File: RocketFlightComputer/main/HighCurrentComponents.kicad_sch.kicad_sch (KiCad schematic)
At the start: 29 parts, among them Q2 SI2302, Q3 SI2302

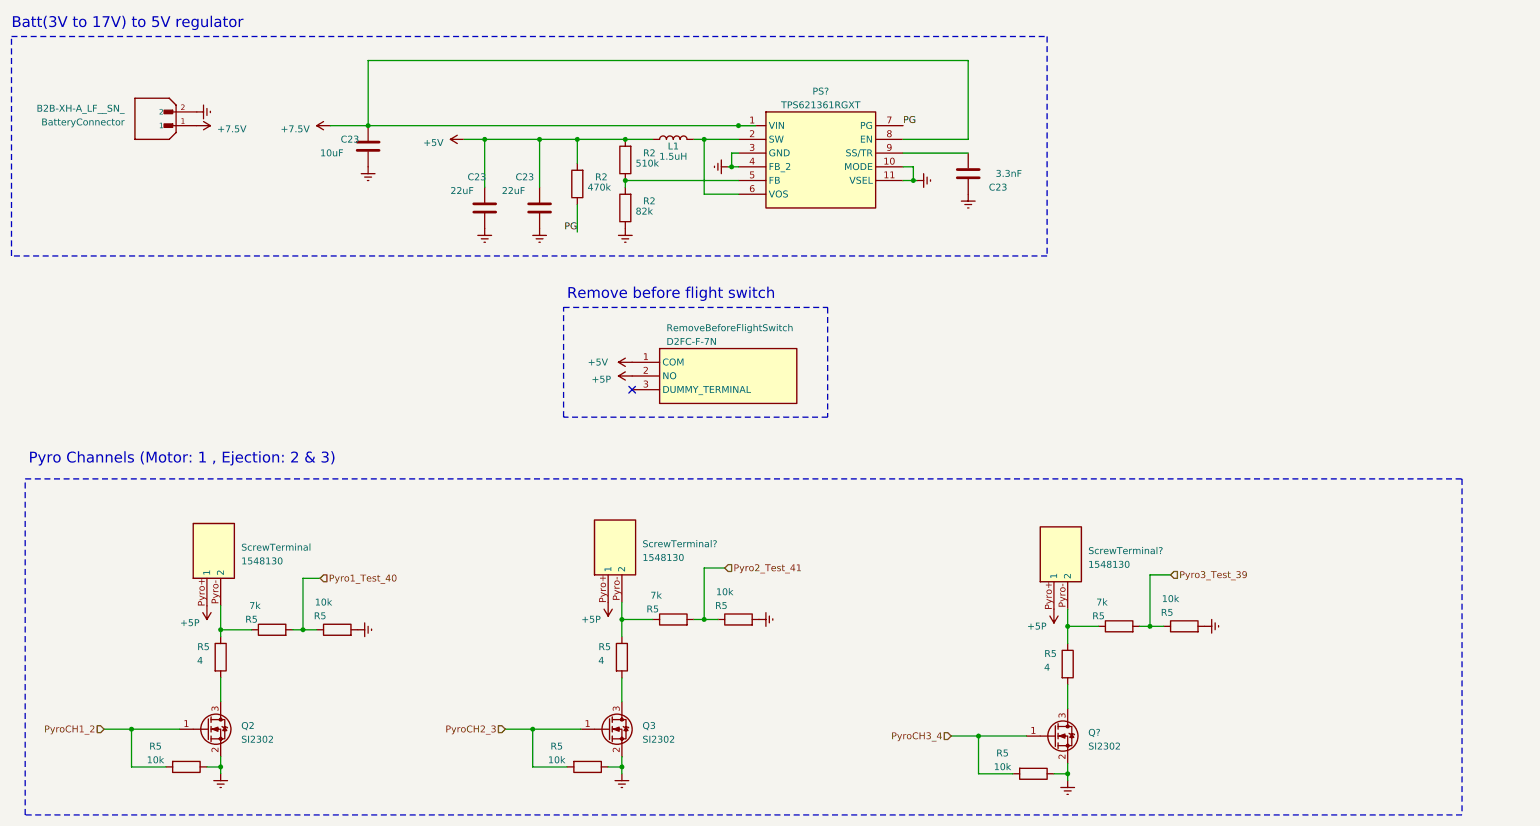
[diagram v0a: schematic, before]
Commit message: Addition of telemetry is pcb schematic
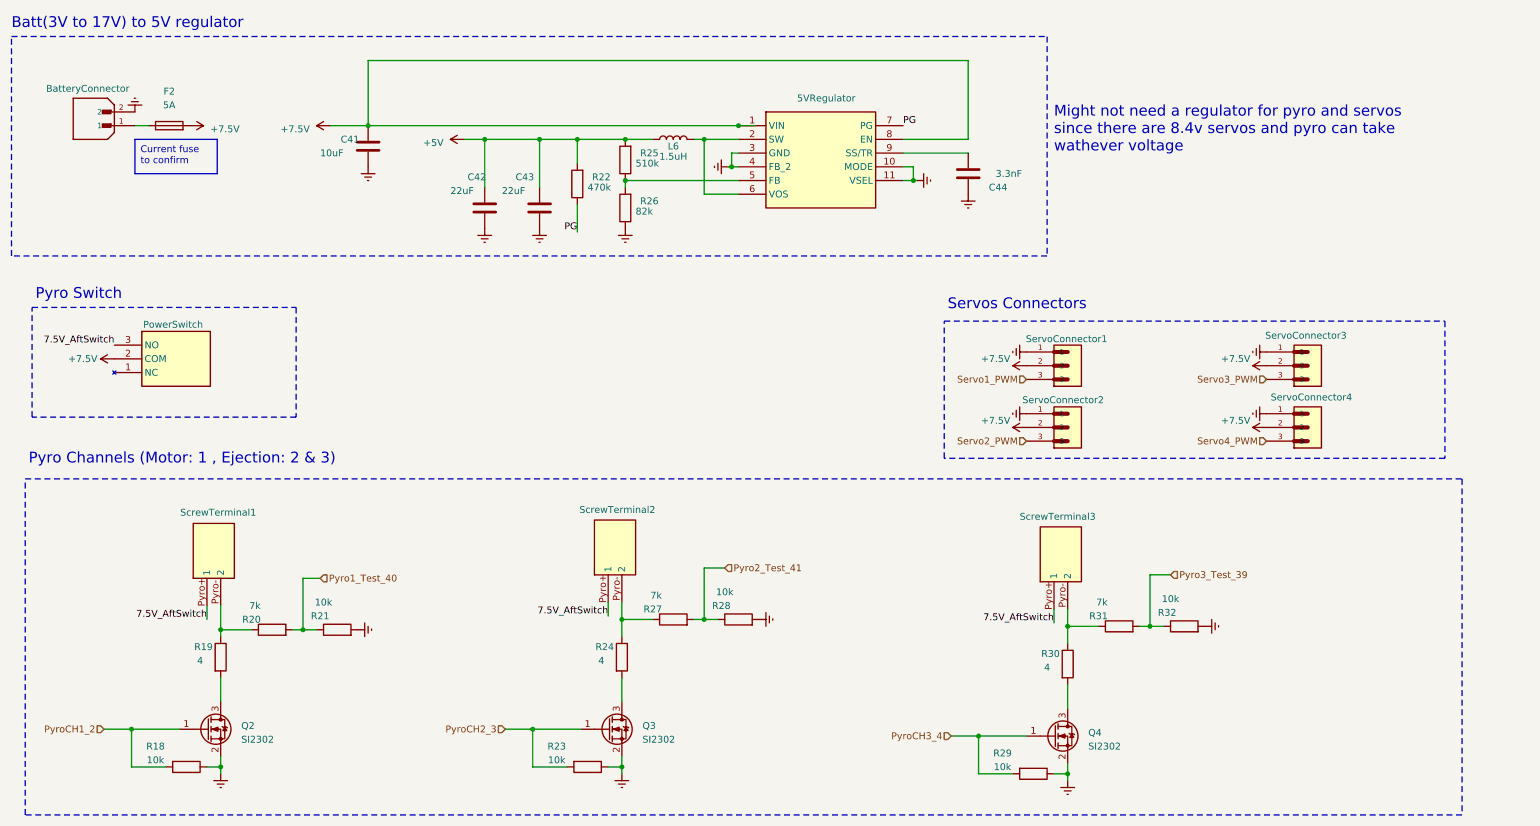
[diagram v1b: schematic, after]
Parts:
- removed RemoveBeforeFlightSwitch: D2FC-F-7N, footprint:D2FCF7N60M, symbol D2FC-F-7N_60M_:D2FC-F-7N_60M_
- added F2: 5A, Resistor_SMD:R_0603_1608Metric_Pad0.98x0.95mm_HandSolder, symbol Device:Fuse
- added PowerSwitch: L102011MS02Q, PowerButton:L102011MS02Q, symbol L102011MS02Q:L102011MS02Q
- added ServoConnector1, ServoConnector2, ServoConnector3, ServoConnector4: B3P-VH_LF__SN_, footprint:JST_B3P-VH_LF__SN_, symbol B3P-VH_LF__SN_:B3P-VH_LF__SN_
- gave numbers to parts that had none: 4
- renumbered C23 to C41, C23 to C42, C23 to C43, C23 to C44, L1 to L6, R5 to R18, R5 to R19, R5 to R20, R5 to R21, R2 to R22, R5 to R23, R5 to R24, R2 to R25, R2 to R26, R5 to R27, R5 to R28, R5 to R29, R5 to R30, R5 to R31, R5 to R32, ScrewTerminal to ScrewTerminal1
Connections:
- net +7.5V: now also F2.2, PowerSwitch.2 (COM), ServoConnector1.2, ServoConnector2.2, ServoConnector3.2, ServoConnector4.2; no longer BatteryConnector.1
- net GNDREF: now also ServoConnector1.1, ServoConnector2.1, ServoConnector3.1, ServoConnector4.1
- net +5P renamed 7.5V_AftSwitch
- net 7.5V_AftSwitch: now also PowerSwitch.3 (NO)
- new net: BatteryConnector.1, F2.1
- new net Servo1_PWM: ServoConnector1.3
- new net Servo2_PWM: ServoConnector2.3
- new net Servo3_PWM: ServoConnector3.3
- new net Servo4_PWM: ServoConnector4.3
- no-connect marks 1 -> 0
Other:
- note added: "Might not need a regulator for pyro and servos since there are 8.4v servos and pyro can take wathever voltage"
- note added: "Pyro Switch"
- note added: "Servos Connectors"
- note removed: "Remove before flight switch"
- moved on the sheet: BatteryConnector

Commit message: The design is getting more mature, still did not choose if doing 4 layers or 2 layers pcb, will try to add 5v for a on board camera and trace routes for reserved pins in case of usage on another vehicle
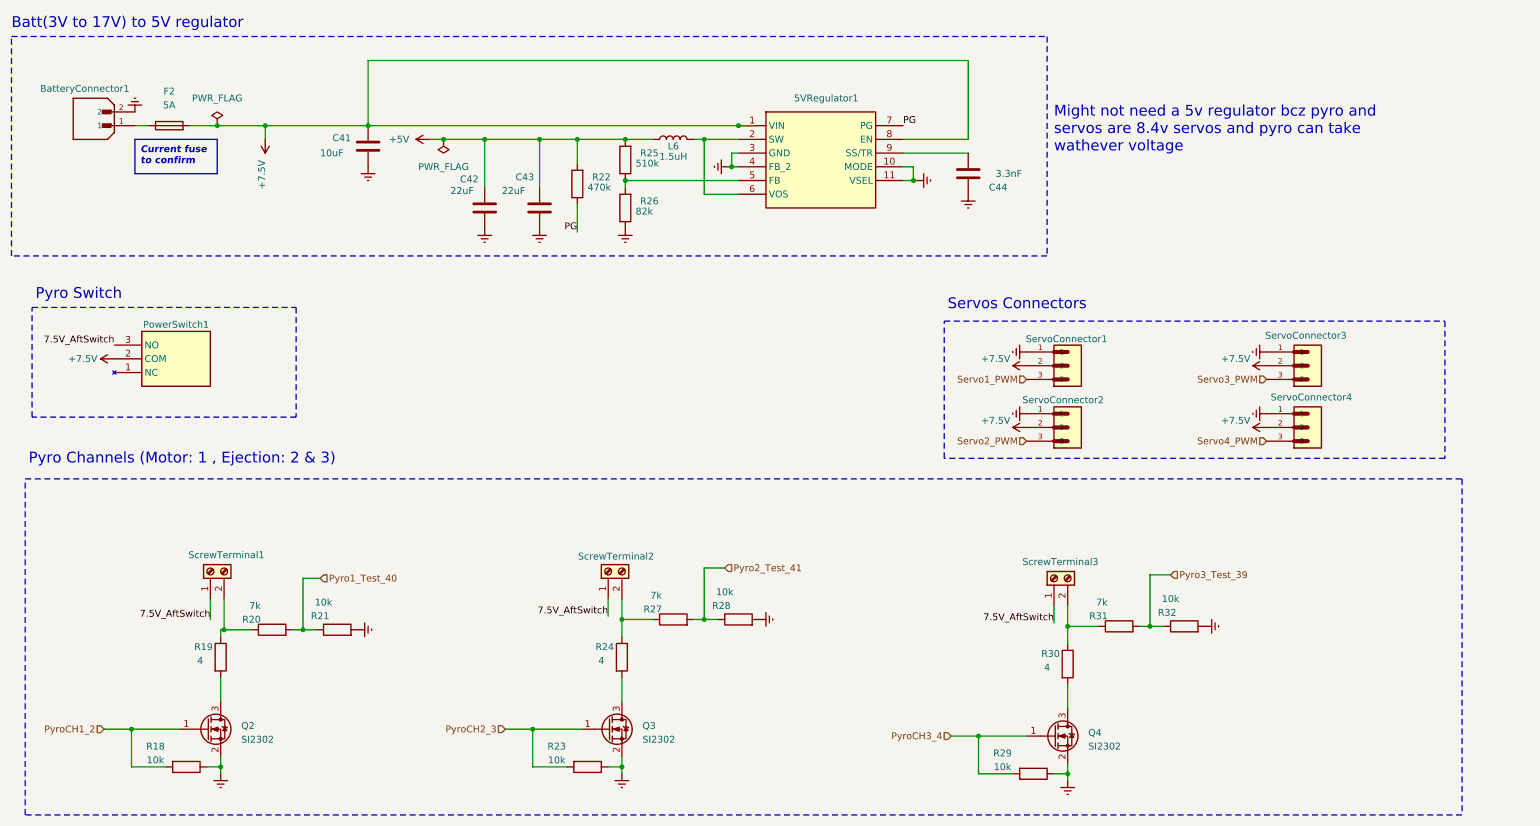
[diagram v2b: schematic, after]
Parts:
- removed ScrewTerminal1, ScrewTerminal2, ScrewTerminal3: 1548130, footprint:1548130, symbol 1548130:1548130
- added ScrewTerminal1, ScrewTerminal2, ScrewTerminal3: Screw_Terminal_01x02, ScrewTerminals:2.54mm, symbol Connector:Screw_Terminal_01x02
- 5VRegulator1: renamed from 5VRegulator; footprint TPS621361RGXT -> footprint:TPS621361RGXT
- L6: footprint (none) -> Resistor_SMD:R_0603_1608Metric_Pad0.98x0.95mm_HandSolder
- renumbered BatteryConnector to BatteryConnector1, PowerSwitch to PowerSwitch1
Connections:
- net 7.5V_AftSwitch: now also ScrewTerminal1.1 (Pyro+), ScrewTerminal2.1 (Pyro+), ScrewTerminal3.1 (Pyro+)
- net at R30.1, R31.1: now also ScrewTerminal3.2 (Pyro-)
- net at R19.1, R20.1: now also ScrewTerminal1.2 (Pyro-)
- net at R24.1, R27.1: now also ScrewTerminal2.2 (Pyro-)
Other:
- note added: "Might not need a 5v regulator bcz pyro and servos are 8.4v servos and pyro can take wathever voltage"
- note removed: "Might not need a regulator for pyro and servos since there are 8.4v servos and pyro can take wathever voltage"

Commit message: Camera and reserve
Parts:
- removed BatteryConnector1: B2B-XH-A_LF__SN_, footprint:JST_B2B-XH-A_LF__SN_, symbol B2B-XH-A_LF__SN_:B2B-XH-A_LF__SN_
- removed PowerSwitch1: L102011MS02Q, PowerButton:L102011MS02Q, symbol L102011MS02Q:L102011MS02Q
- added BatteryConnector1: XT30UPB-M, XT30:AMASS_XT30UPB-M, symbol xt30:XT30UPB-M
- added ScrewTerminal4: Screw_Terminal_01x02, ScrewTerminals:2.54mm, symbol Connector:Screw_Terminal_01x02
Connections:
- net +7.5V: now also ScrewTerminal4.2 (Pyro-); no longer F2.2
- net 7.5V_AftSwitch: now also ScrewTerminal4.1 (Pyro+)
- net GNDREF: now also BatteryConnector1.N
- net at F2.1: now also BatteryConnector1.P
- new net +BATT: F2.2

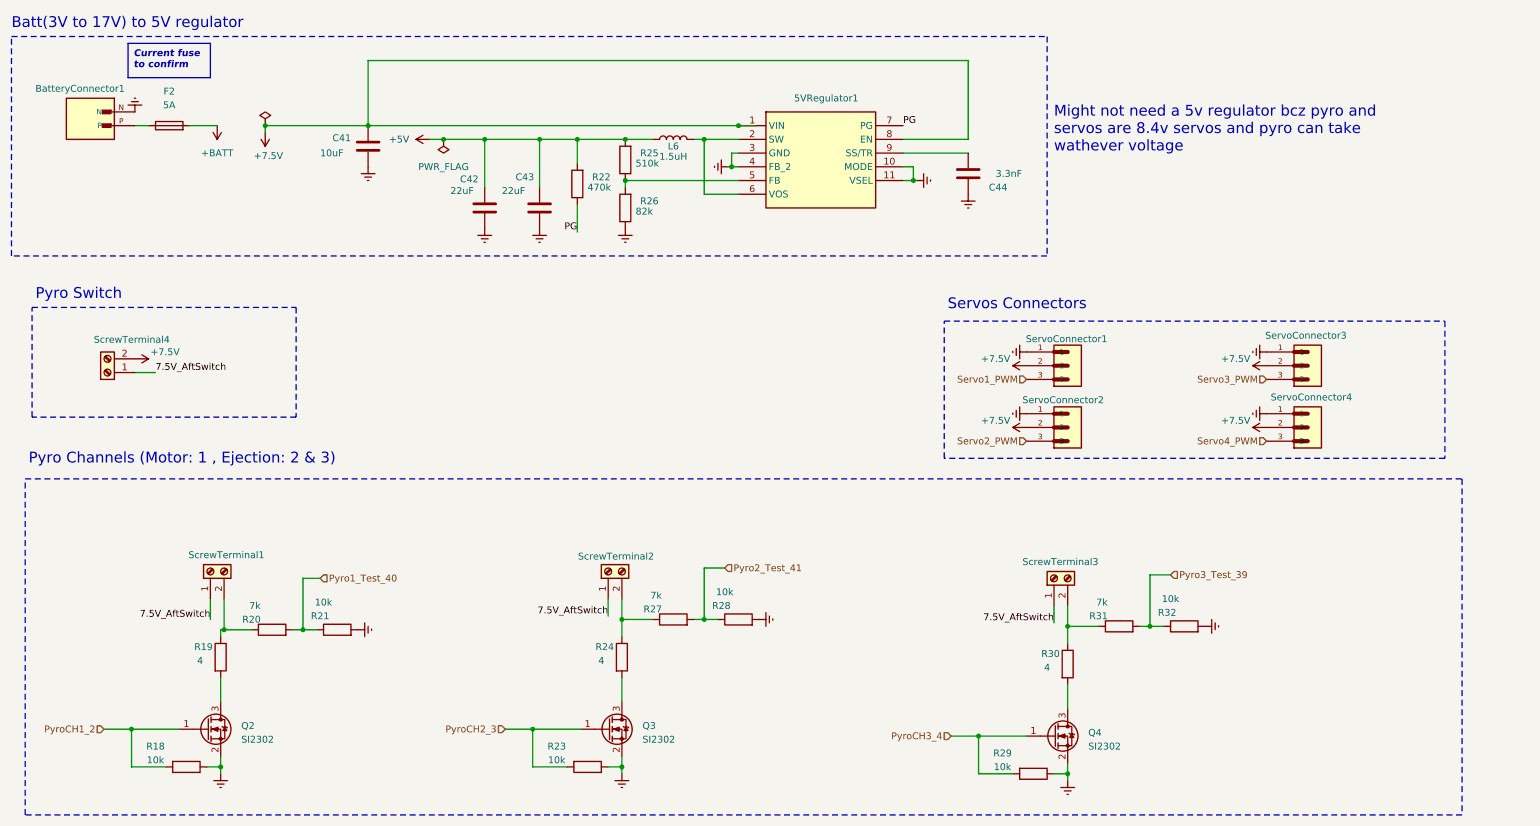
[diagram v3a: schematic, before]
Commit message: CID documentation and started the PCB editor process
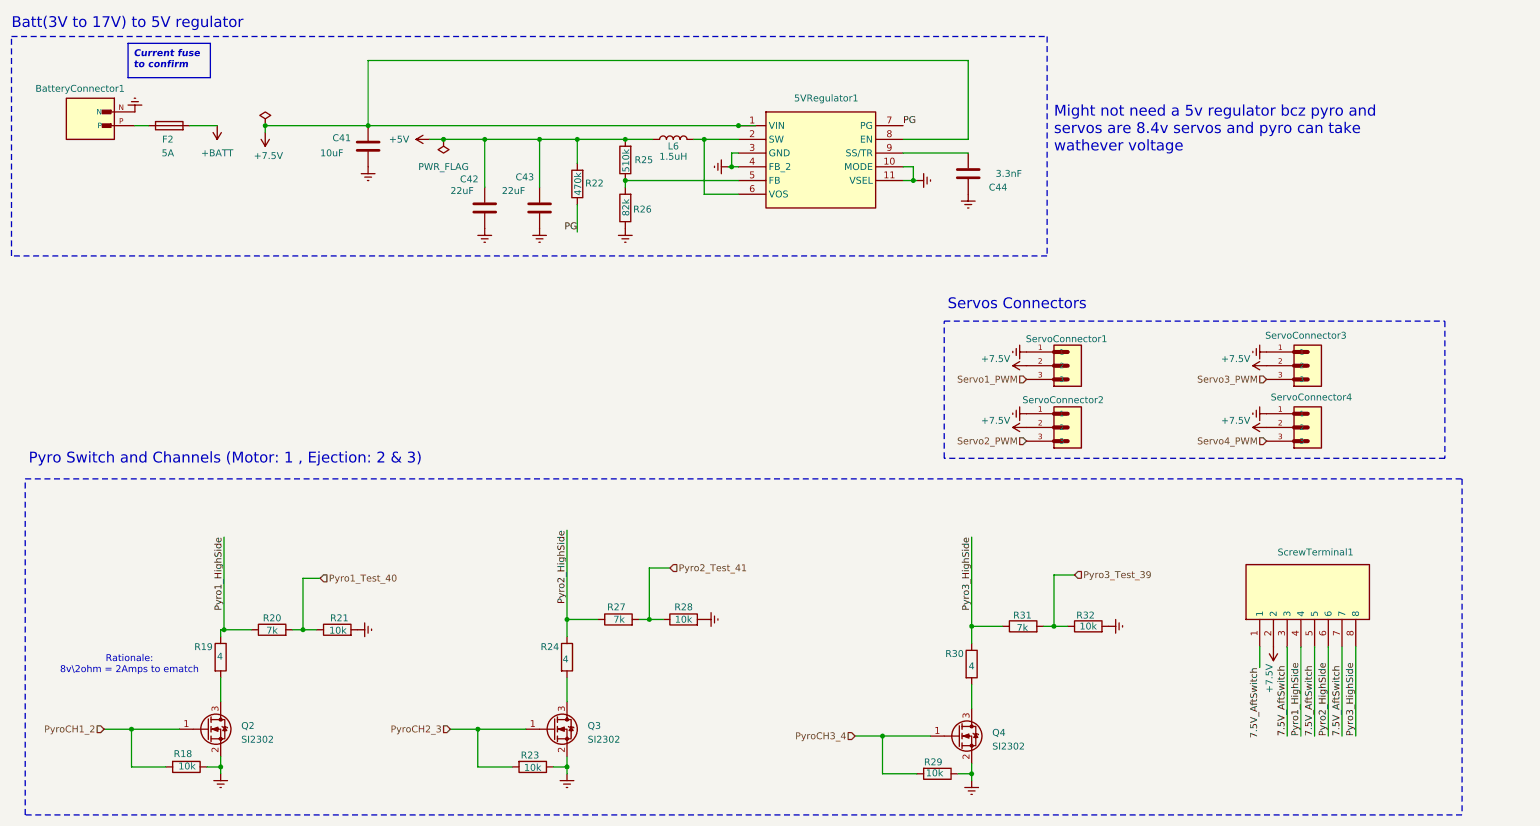
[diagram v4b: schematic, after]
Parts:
- removed ScrewTerminal1, ScrewTerminal2, ScrewTerminal3, ScrewTerminal4: Screw_Terminal_01x02, ScrewTerminals:2.54mm, symbol Connector:Screw_Terminal_01x02
- added ScrewTerminal1: 1725711, footprint:1725711, symbol 1725711:1725711
- ServoConnector1, ServoConnector2, ServoConnector4: value B3P-VH_LF__SN_ -> ~; footprint footprint:JST_B3P-VH_LF__SN_ -> Connector_JST:JST_GH_BM03B-GHS-TBT_1x03-1MP_P1.25mm_Vertical; Availability In Stock -> (none); Check_prices https://www.snapeda.com/parts/B3P-VH(LF)(SN)/JST+Sales+Amer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 -> (none); MANUFACTURER JST -> (none); MF JST Sales -> (none); MP B3P-VH(LF)(SN) -> (none); Package None -> (none); Price None -> (none); SnapEDA_Link https://www.snapeda.com/parts/B3P-VH(LF)(SN)/JST+Sales+Amer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 -> (none)
- ServoConnector3: value B3P-VH_LF__SN_ -> ~; footprint footprint:JST_B3P-VH_LF__SN_ -> Connector_JST:JST_GH_BM03B-GHS-TBT_1x03-1MP_P1.25mm_Vertical; Availability In Stock -> (none); Check_prices https://www.snapeda.com/parts/B3P-VH(LF)(SN)/JST+Sales+Amer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 -> (none); MF JST Sales -> (none); MP B3P-VH(LF)(SN) -> (none); Package None -> (none); Price None -> (none); SnapEDA_Link https://www.snapeda.com/parts/B3P-VH(LF)(SN)/JST+Sales+Amer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 -> (none)
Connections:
- net +7.5V: now also ScrewTerminal1.2
- net 7.5V_AftSwitch: now also ScrewTerminal1.1, ScrewTerminal1.3, ScrewTerminal1.5, ScrewTerminal1.7
- net Pyro3_HighSide: now reaches R30.1, R31.1
- net Pyro3_HighSide: now also ScrewTerminal1.8
- net Pyro1_HighSide: now reaches R19.1, R20.1
- net Pyro1_HighSide: now also ScrewTerminal1.4
- net Pyro2_HighSide: now reaches R24.1, R27.1
- net Pyro2_HighSide: now also ScrewTerminal1.6
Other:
- note added: "Pyro Switch and Channels (Motor: 1 , Ejection: 2 & 3)"
- note added: "Rationale: 8v\2ohm = 2Amps to ematch"
- note removed: "Pyro Channels (Motor: 1 , Ejection: 2 & 3)"
- note removed: "Pyro Switch"
- moved on the sheet: Q3, Q4, R23, R24, R27, R28, R29, R30, R31, R32

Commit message: Layout of PCB mostly done
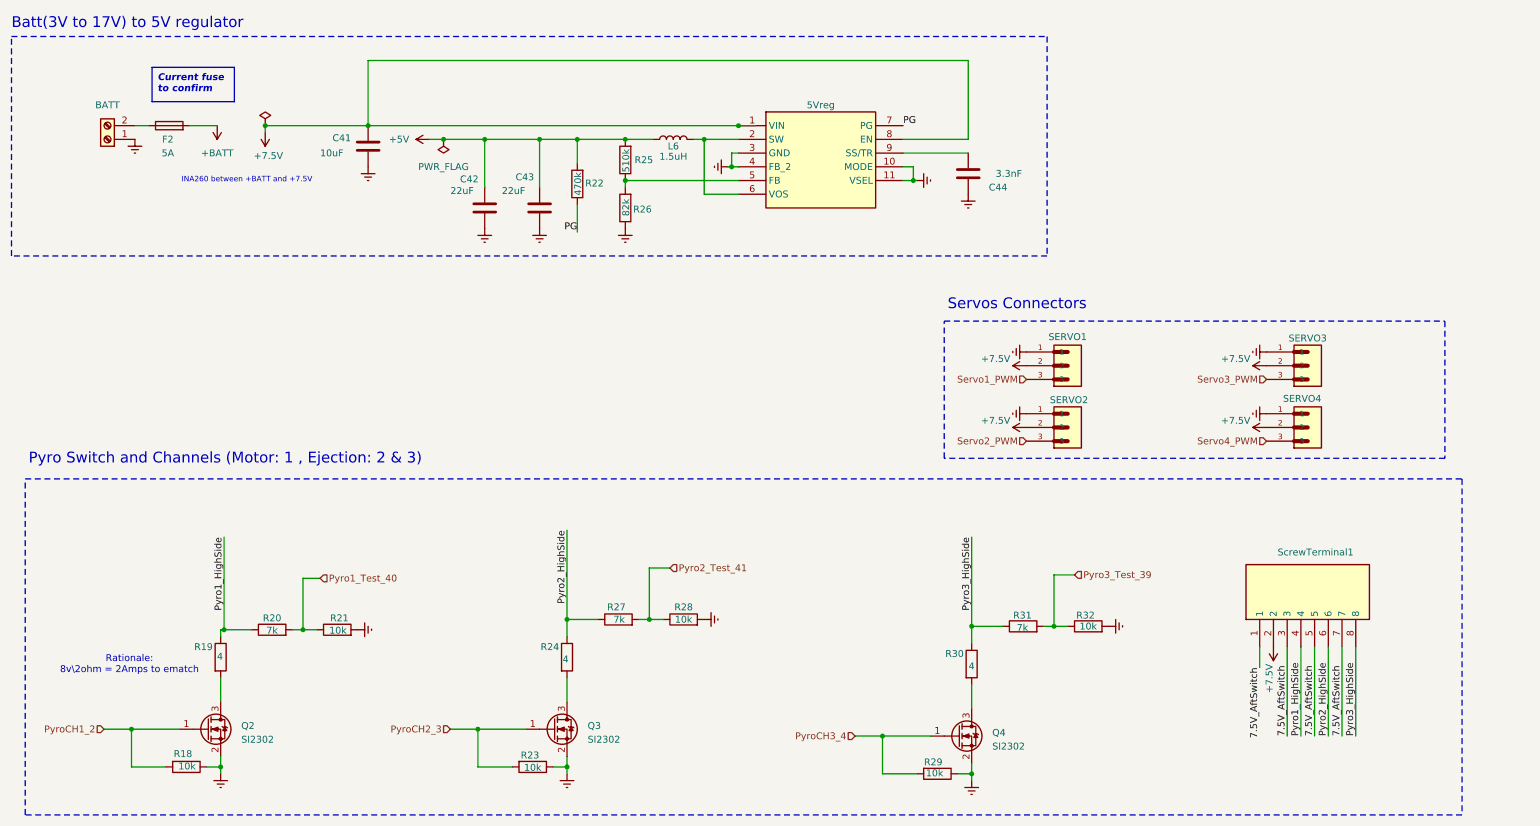
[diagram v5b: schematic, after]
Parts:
- removed BatteryConnector1: XT30UPB-M, XT30:AMASS_XT30UPB-M, symbol xt30:XT30UPB-M
- added J1: BATT, footprint:1725656, symbol Connector:Screw_Terminal_01x02
- F2: footprint Resistor_SMD:R_0603_1608Metric_Pad0.98x0.95mm_HandSolder -> Fuse:Fuse_0603_1608Metric
- SERVO1: renamed from ServoConnector1; value ~ -> SERVO1
- SERVO2: renamed from ServoConnector2; value ~ -> SERVO2
- SERVO3: renamed from ServoConnector3; value ~ -> SERVO3
- SERVO4: renamed from ServoConnector4; value ~ -> SERVO4
- TPS621361RGXT1: renamed from 5VRegulator1; value TPS621361RGXT -> 5Vreg
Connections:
- net GNDREF: now also J1.1 (Pin_1)
- net at F2.1: now also J1.2 (Pin_2)
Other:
- note added: "INA260 between +BATT and +7.5V"
- note removed: "Might not need a 5v regulator bcz pyro and servos are 8.4v servos and pyro can take wathever voltage"
